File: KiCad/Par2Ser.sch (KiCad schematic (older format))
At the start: 37 parts, among them J1 DB25_Male, J2 USB_C_Receptacle_USB2.0, J3 Conn_02x05_Odd_Even, U1 LC4032V-5TN48C, U2 FT240XS-R

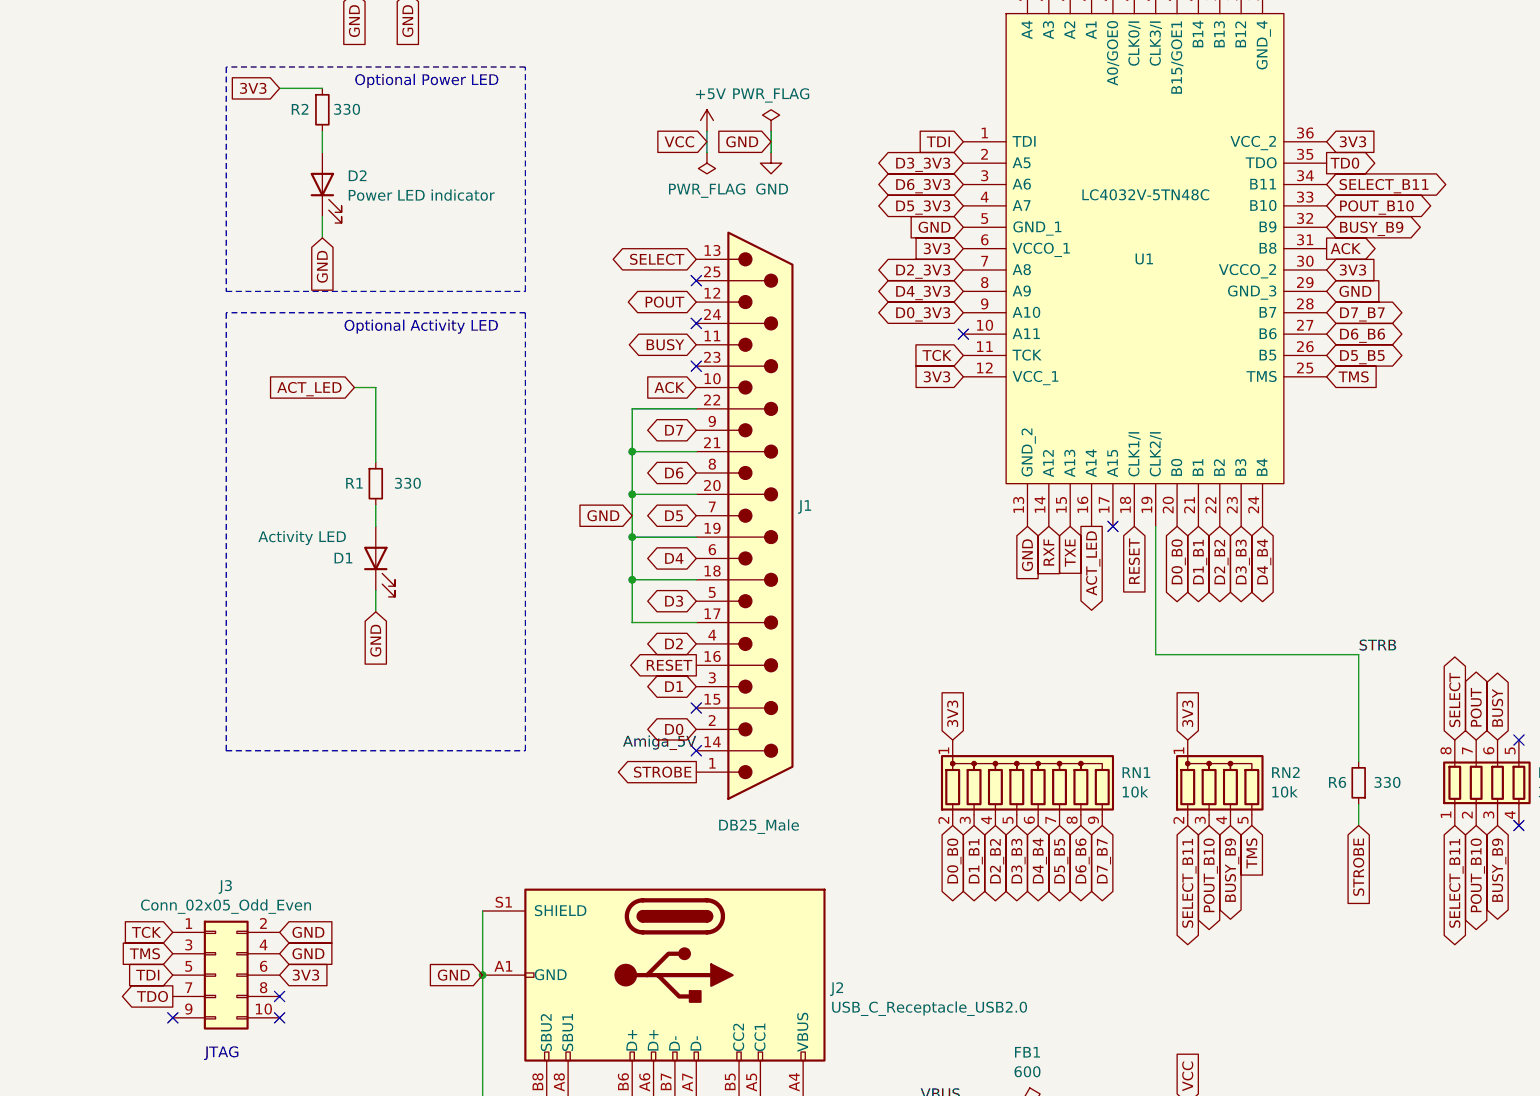
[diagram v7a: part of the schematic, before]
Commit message: Add 4.7k pull-down resistor on TCK and route all JTAG traces
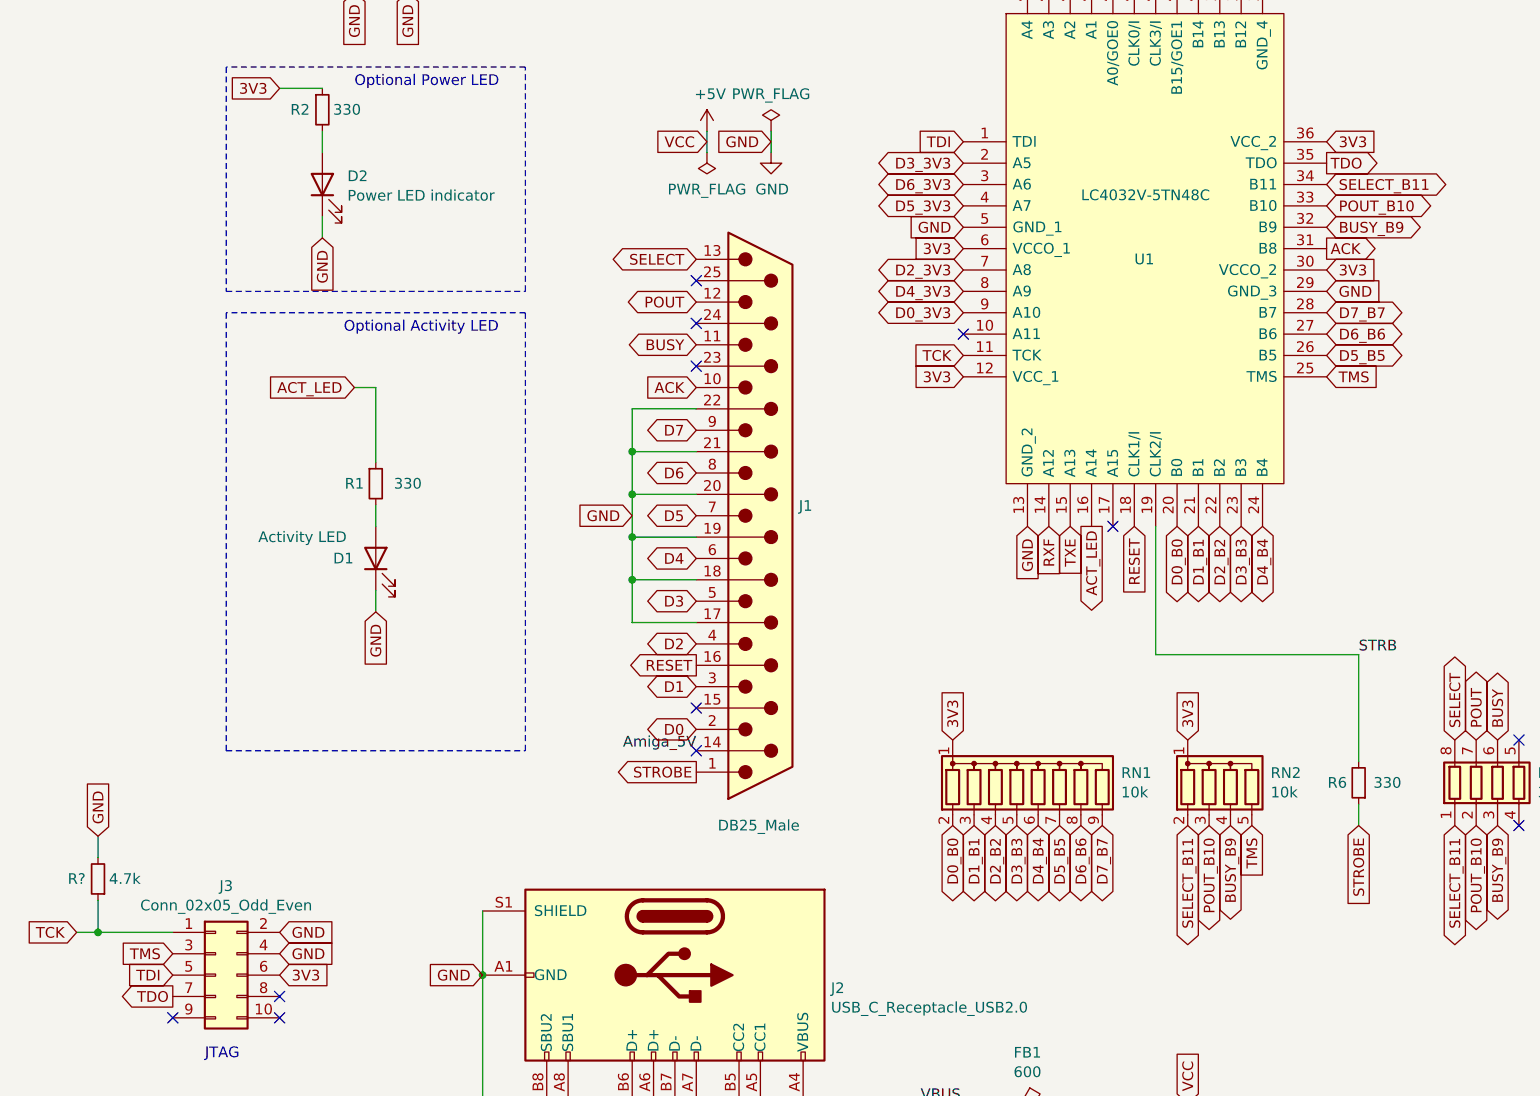
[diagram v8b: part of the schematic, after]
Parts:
- added R?: 4.7k, Resistor_SMD:R_0805_2012Metric_Pad1.20x1.40mm_HandSolder, symbol Device:R_Small
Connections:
- net TD0 is gone; now on net TDO: U1.35 (TDO)
- net GND: now also R?.2
- net TCK: now also R?.1
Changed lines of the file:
@@
 TDI
 Text GLabel 6700 2550 2    50   Output ~ 0
-TD0
+TDO
 Text GLabel 6700 3550 2    50   Input ~ 0
 TMS
@@
 	1    0    0    -1
 $EndComp
-Text GLabel 1300 6150 0    50   Input ~ 0
+Text GLabel 850  6150 0    50   Input ~ 0
 TCK
 Text GLabel 1300 6250 0    50   Input ~ 0
@@
 Text Notes 1450 6750 0    50   ~ 0
 JTAG
+$Comp
+L Device:R_Small R?
+U 1 1 6A16EF59
+P 950 5900
+F 0 "R?" H 1050 5900 50  0000 C CNN
+F 1 "4.7k" H 750 5900 50  0000 L CNN
+F 2 "Resistor_SMD:R_0805_2012Metric_Pad1.20x1.40mm_HandSolder" H 950 5900 50  0001 C CNN
+F 3 "~" H 950 5900 50  0001 C CNN
+	1    950  5900
+	-1   0    0    1
+$EndComp
+Text GLabel 950  5700 1    50   Input ~ 0
+GND
+Wire Wire Line
+	950  5700 950  5800
+Wire Wire Line
+	850  6150 950  6150
+Wire Wire Line
+	950  6000 950  6150
+Connection ~ 950  6150
+Wire Wire Line
+	950  6150 1300 6150
 $EndSCHEMATC
